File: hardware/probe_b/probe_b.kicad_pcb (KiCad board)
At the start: 2 copper layers, 81 x 20 mm, 30 parts, among them J1 TEST_1P, J3 TEST_1P, J4 TEST_1P, J5 TEST_1P, J7 Conn_01x04, Q1 SI3415, U1 ATTINY25-20PU

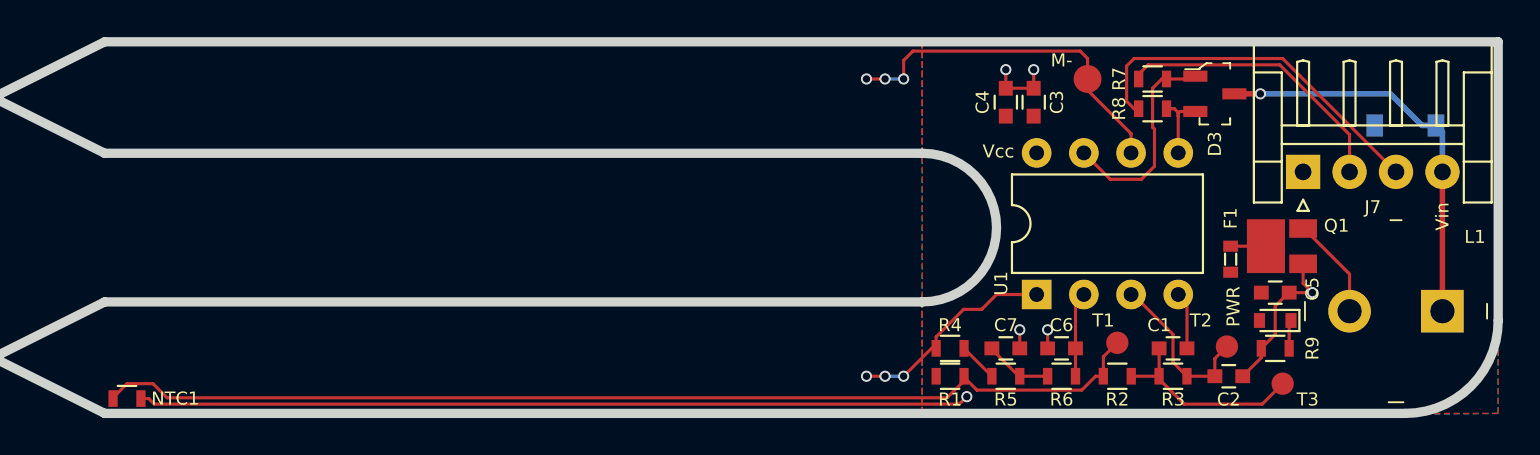
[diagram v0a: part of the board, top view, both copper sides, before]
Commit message: Fixes #21. Also removes RC filters that made the output impedence too high for the ADC. Changed connector to Micro USB due to cable availabiliy. Changed to a more reasonable inline ferrite and also removed ptc fuse due to too high Vdrop. Series resistors for I2C righ-sized.
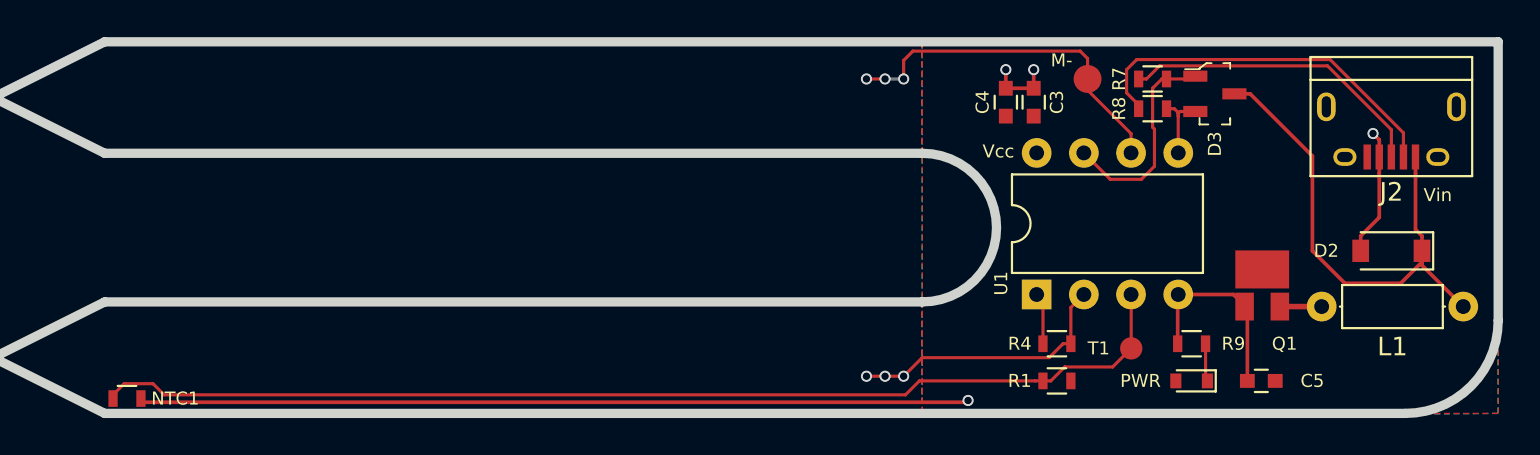
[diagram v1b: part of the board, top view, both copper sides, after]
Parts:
- removed C1, C2, C6, C7: 100nF, Capacitors_SMD:C_0603
- removed F1: Polyfuse_Small, digikey-footprints:0603
- removed J4, J5: TEST_1P, Measurement_Points:Measurement_Point_Round-SMD-Pad_Small
- removed J7: Conn_01x04, Connectors_JST:JST_EH_S04B-EH_04x2.50mm_Angled
- removed R2, R3, R5, R6: 100K, Resistors_SMD:R_0603
- added J2: USB_A, Connect:USB_Micro-B, F.Cu at (245.2, 104.8)
- D1: value LED -> PWR_LED
- D2: value D_Zener -> BZT52C5V6; moved to F.Cu
- D3: value BAT54C-7-F -> BAT54C
- L1: footprint digikey-footprints:Inductor_13R106C -> Inductors_THT:L_Axial_L5.3mm_D2.2mm_P7.62mm_Horizontal_Vishay_IM-1
- Q1: value SI3415 -> SI2323DS
- R1: value 10K -> 15K
- R7, R8: value R -> 33R
- R9: value 2K -> 1K
- moved D2 6.79 mm to (245.2, 111.2)
- moved R1 5.76 mm to (227.2, 118.2), turned to 180 degrees
- moved R4 5.76 mm to (227.2, 116.2)
- moved D1 5.55 mm to (234.5, 118.2)
- moved C5 4.81 mm to (238.2, 118.2), turned to 180 degrees
- moved R9 4.51 mm to (234.5, 116.2)
- moved L1 3.63 mm to (249.1, 114.2)
- moved Q1 2.55 mm to (238.3, 113.2), turned to 90 degrees
- moved J1 0.81 mm to (231.2, 116.5)
- moved G*** 0.34 mm to (231.5, 109.8)
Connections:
- J1 pad 1: Net-(J1-Pad1) -> TEMP_A
- NTC1 pad 1: Net-(J1-Pad1) -> TEMP_A
- Q1 pad 3: Net-(F1-Pad1) -> Vcc
- R1 pad 2: Net-(J1-Pad1) -> TEMP_A
- R4 pad 2: Net-(R4-Pad2) -> MOIST_A
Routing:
- net Net-(J1-Pad1): track 57.4 -> 0.00 mm
- net TEMP_A: track 9.08 -> 59.5 mm
- net MOIST_A: track 4.59 -> 15.6 mm, vias 0 -> 3
- net Net-(C1-Pad1): track 10.8 -> 0.00 mm
- net MOIST+: track 11.3 -> 3.04 mm, vias 3 -> 0
- net Vin: track 21.7 -> 27.7 mm, vias 1 -> 0
- net GND: track 61.9 -> 66.5 mm, vias 6 -> 4
- net Net-(C7-Pad1): track 3.65 -> 0.00 mm
- net Net-(L1-Pad2): track 5.51 -> 2.25 mm
- net Net-(R4-Pad2): track 2.12 -> 0.00 mm
- net Net-(F1-Pad1): track 1.90 -> 0.00 mm
- net Net-(J2-Pad3): track 15.4 -> 16.8 mm
- net Net-(J2-Pad2): track 19.9 -> 20.4 mm
- net Net-(D1-Pad1): track 1.54 -> 2.04 mm
- added copper zone on B.Cu, net MOIST_A
- added copper zone on F.Cu, net MOIST_A
- removed copper zone on B.Cu, net MOIST+
- removed copper zone on F.Cu, net MOIST+
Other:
- net class POWER: clearance 0.4 -> 0.2; trace_width 0.3 -> 0.2
- board text removed: "T2"
- board text removed: "T3"

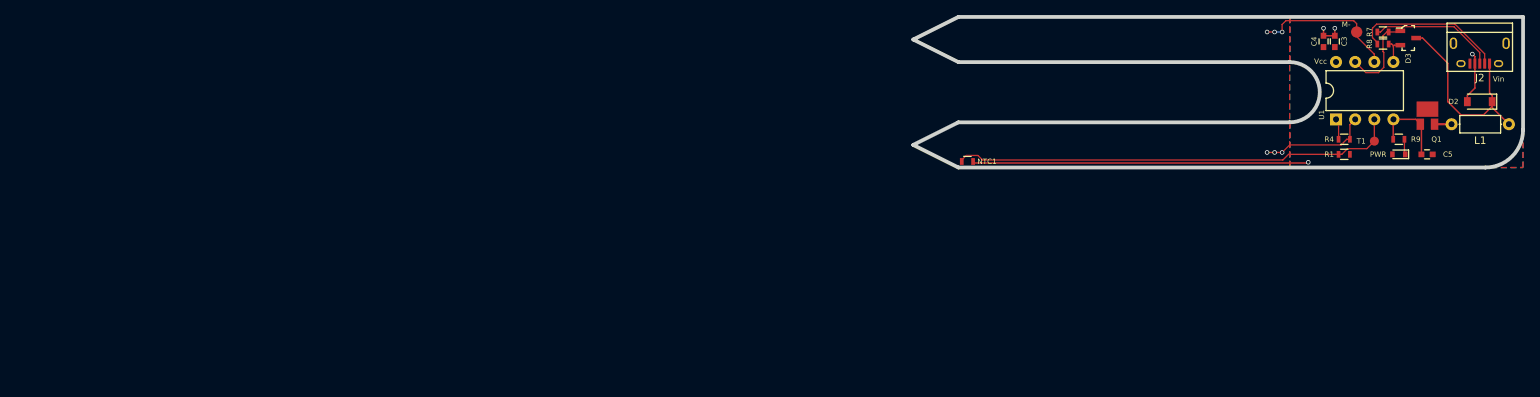
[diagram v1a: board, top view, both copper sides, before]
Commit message: Upgrading project to kicad 5.0 and fixing some issues with the last revision.
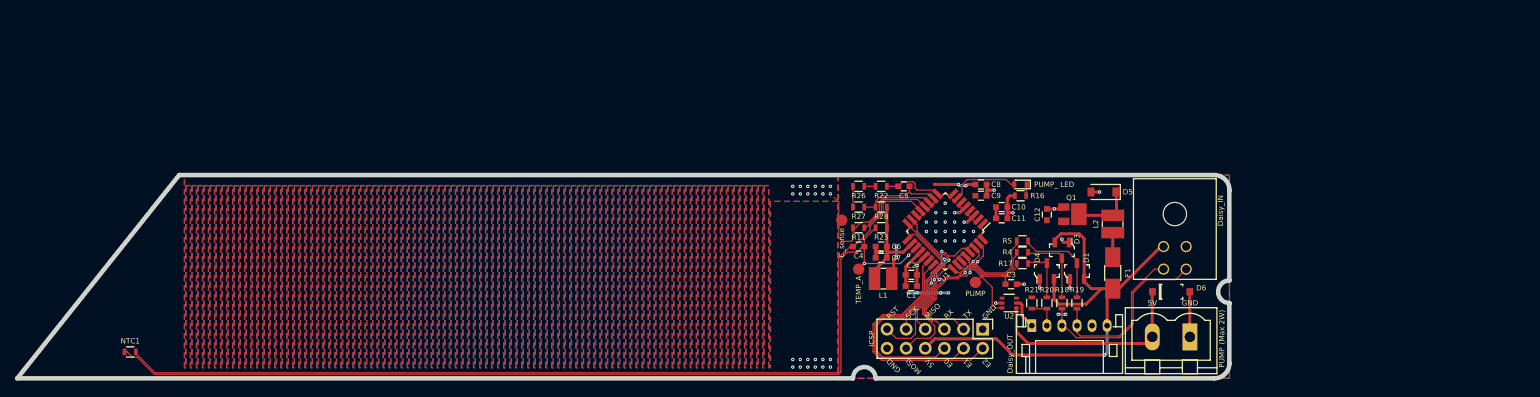
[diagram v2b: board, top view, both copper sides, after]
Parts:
- removed the G*** at (231.5, 109.8)
- removed R1: 15K, Resistors_SMD:R_0603
- removed R7, R8: 33R, Resistors_SMD:R_0603
- removed R9: 1K, Resistors_SMD:R_0603
- added C1: 10nF, Capacitors_SMD:C_0603, F.Cu at (169.8, 135.8)
- added C10: 10nF, Capacitors_SMD:C_0603, F.Cu at (181.8, 125.2)
- added C11: 100nF, Capacitors_SMD:C_0603, F.Cu at (181.8, 126.8)
- added C12: 1µF, Capacitors_SMD:C_0603, F.Cu at (187.8, 126.2)
- added C2: 100nF, Capacitors_SMD:C_0603, F.Cu at (169.8, 134.2)
- added C6: 10nF, Capacitors_SMD:C_0603, F.Cu at (165.8, 130.5)
- added C7: 100nF, Capacitors_SMD:C_0603, F.Cu at (165.8, 132.0)
- added C8: 100nF, Capacitors_SMD:C_0603, F.Cu at (179.0, 122.2)
- added C9: 10nF, Capacitors_SMD:C_0603, F.Cu at (179.0, 123.8)
- added D4: BAT54S-7-F, digikey-footprints:SOT-23-3, F.Cu at (187.8, 133.8)
- added D5: BZT52C5V6, Diodes_SMD:D_SOD-123, F.Cu at (195.2, 123.2)
- added D6: MBR0520LT1G, digikey-footprints:SOD-123, F.Cu at (204.2, 136.5)
- added F1: 0ZCJ0050FF2G, Fuse_Holders_and_Fuses:Fuse_SMD1206_HandSoldering, F.Cu at (196.5, 134.0)
- added G***: LOGO, emilibeda:waterino_8x16mm, B.Cu at (193.0, 130.2)
- added G***: LOGO, emilibeda:OSH_6mm, B.Cu at (156.5, 141.5)
- added J4: C_sense, Measurement_Points:Measurement_Point_Round-SMD-Pad_Small, F.Cu at (160.5, 127.0)
- added J5: Daisy_OUT, Connectors_JST:JST_PH_S6B-PH-K_06x2.00mm_Angled, F.Cu at (185.8, 141.0)
- added J6: Daisy_IN, Connectors_Molex:Molex_Microfit3_Header_02x02_Angled_43045-040x, F.Cu at (203.2, 130.5)
- added J7: TEMP_A, Measurement_Points:Measurement_Point_Round-SMD-Pad_Small, F.Cu at (162.8, 133.5)
- added L2: 10uH, digikey-footprints:1210, F.Cu at (196.5, 127.5)
- added R11: 1M, Resistors_SMD:R_0603, F.Cu at (162.8, 128.0)
- added R16: 1K, Resistors_SMD:R_0603, F.Cu at (184.2, 123.8)
- added R17: 150R, Resistors_SMD:R_0603, F.Cu at (184.5, 132.8)
- added R18: 150R, Resistors_SMD:R_0603, F.Cu at (189.8, 138.0)
- added R19: 150R, Resistors_SMD:R_0603, F.Cu at (191.8, 138.0)
- added R20: 150R, Resistors_SMD:R_0603, F.Cu at (187.8, 138.0)
- added R21: 10K, Resistors_SMD:R_0603, F.Cu at (185.8, 138.0)
- added R22: 100K, Resistors_SMD:R_0603, F.Cu at (165.8, 122.5)
- added R23: 15K, Resistors_SMD:R_0603, F.Cu at (165.8, 128.0)
- added R26: 100K, Resistors_SMD:R_0603, F.Cu at (162.8, 122.5)
- added R27: 100K, Resistors_SMD:R_0603, F.Cu at (162.8, 125.2)
- added R28: 100K, Resistors_SMD:R_0603, F.Cu at (165.8, 125.2)
- added R5: 150R, Resistors_SMD:R_0603, F.Cu at (184.5, 129.8)
- added U2: MIC94090, TO_SOT_Packages_SMD:SOT-363_SC-70-6, F.Cu at (182.8, 138.0)
- C5: value 1µF -> 100nF
- D1: value PWR_LED -> BAT54S-7-F; footprint Diodes_SMD:D_0603 -> digikey-footprints:SOT-23-3
- D2: value BZT52C5V6 -> PUMP_ LED; footprint Diodes_SMD:D_SOD-123 -> Diodes_SMD:D_0603
- D3: value BAT54C -> BAT54S-7-F
- J1: value TEST_1P -> ICSP; footprint Measurement_Points:Measurement_Point_Round-SMD-Pad_Small -> Pin_Headers:Pin_Header_Straight_2x06_Pitch2.54mm
- J2: value USB_A -> PUMP; footprint Connect:USB_Micro-B -> Measurement_Points:Measurement_Point_Round-SMD-Pad_Small
- J3: value TEST_1P -> PUMP; footprint Measurement_Points:Measurement_Point_Round-SMD-Pad_Small -> emilibeda:PhoenixContact_MSTBVA-G_02x5.00mm_Vertical
- L1: value L -> 10uH; footprint Inductors_THT:L_Axial_L5.3mm_D2.2mm_P7.62mm_Horizontal_Vishay_IM-1 -> digikey-footprints:1210
- R4: value 10K -> 150R
- U1: value ATTINY25-20PU -> ATMEGA328P-AU; footprint Housings_DIP:DIP-8_W7.62mm -> Housings_QFP:TQFP-32_7x7mm_Pitch0.8mm
- moved NTC1 114.0 mm to (66.0, 144.5)
- moved L1 85.6 mm to (166.0, 134.8)
- moved J2 73.6 mm to (178.2, 135.2), turned to 0 degrees
- moved C5 69.6 mm to (168.8, 122.5)
- moved C4 67.5 mm to (162.8, 130.5), turned to 0 degrees
- moved D2 62.0 mm to (184.2, 122.2)
- moved J1 57.7 mm to (179.2, 141.5), turned to 270 degrees
- moved U1 54.0 mm to (174.2, 128.5), turned to 225 degrees
- moved D3 54.0 mm to (189.8, 131.0), turned to 270 degrees
- moved C3 53.8 mm to (183.0, 135.5), turned to 0 degrees
- moved Q1 49.0 mm to (191.0, 126.2), turned to 0 degrees
- moved J3 46.2 mm to (206.8, 142.5), turned to 180 degrees
- moved D1 45.5 mm to (191.8, 133.8), turned to 90 degrees
- moved R4 45.3 mm to (184.5, 131.2), turned to 180 degrees
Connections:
- C3 pad 1: Vcc -> OVRFLW_SENSE
- C4 pad 1: Vcc -> ~TEMP_EXC
- C4 pad 2: GND -> TEMP+
- C5 pad 1: Vcc -> RC_REF
- C5 pad 2: GND -> ~RC_EXC
- D1 pad 1: Net-(D1-Pad1) -> GND
- D1 pad 2: Vcc -> Vin
- D2 pad 1: Vin -> Net-(D2-Pad1)
- D2 pad 2: GND -> PWRLED
- D3 pad 1: SCL -> GND
- D3 pad 2: SDA -> Vin
- D3 pad 3: Vin -> Net-(D3-Pad3)
- J1 pad 1: TEMP_A -> GND
- J2 pad 1: Vin -> PUMP
- J3 pad 1: MOIST- -> GND
- L1 pad 1: Vin -> Vcc
- L1 pad 2: Net-(L1-Pad2) -> AVcc
- NTC1 pad 1: TEMP_A -> TEMP+
- NTC1 pad 2: GND -> ~TEMP_EXC
- Q1 pad 2: Net-(L1-Pad2) -> Vcc
- Q1 pad 3: Vcc -> Net-(D5-Pad1)
- R4 pad 1: MOIST+ -> Net-(D3-Pad3)
- R4 pad 2: MOIST_A -> SDA
- U1 pad 1: MOIST+ -> Net-(U1-Pad1)
- U1 pad 2: MOIST_A -> Net-(U1-Pad2)
- U1 pad 3: TEMP_A -> GND
- U1 pad 4: GND -> Vcc
- U1 pad 5: SDA -> GND
- U1 pad 6: MOIST- -> Vcc
- U1 pad 7: SCL -> PWRLED
- U1 pad 8: Vcc -> Net-(U1-Pad8)
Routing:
- net TEMP+: track 0.00 -> 129.5 mm, vias 0 -> 2
- net ~TEMP_EXC: track 0.00 -> 125.5 mm
- net TEMP_A: track 59.5 -> 0.00 mm
- net Vin: track 27.7 -> 68.5 mm, vias 0 -> 1
- net DBG_A2: track 0.00 -> 32.2 mm
- net DBG_A1: track 0.00 -> 29.0 mm
- net Net-(D6-PadK): track 0.00 -> 28.3 mm
- net Net-(J5-Pad3): track 0.00 -> 25.6 mm
- net DBG_A0: track 0.00 -> 25.6 mm
- net GND: track 66.5 -> 41.0 mm, vias 4 -> 42
- net MOSI: track 0.00 -> 24.5 mm, vias 0 -> 2
- net /Csense: track 0.00 -> 23.2 mm, vias 0 -> 12
- net RST: track 0.00 -> 21.5 mm, vias 0 -> 2
- net Net-(J5-Pad4): track 0.00 -> 21.0 mm
- net Net-(J2-Pad2): track 20.4 -> 0.00 mm
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- added copper zone on B.Cu, net /Csense
- added copper zone on F.Cu, net /Csense
- added copper zone on F.Cu, net GND
- removed copper zone on B.Cu, net MOIST-
- removed copper zone on F.Cu, net MOIST-
- removed copper zone on B.Cu, net MOIST_A
- removed copper zone on F.Cu, net MOIST_A
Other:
- board size 81 x 20 mm -> 161 x 27 mm
- net class Default: clearance 0.17 -> 0.11; trace_width 0.17 -> 0.11; via_dia 0.6 -> 0.45; via_drill 0.4 -> 0.2
- net class POWER removed
- net class Power added: clearance 0.15, trace_width 0.4, via_dia 0.45, via_drill 0.2
- rule pad_to_mask_clearance: 0.01 -> 0
- rule trace_clearance: 0.17 -> 0.11
- rule trace_min: 0.16 -> 0.11
- rule via_min_drill: 0.3 -> 0.2
- rule via_min_size: 0.4 -> 0.45
- board text added: "(Max 2W)"
- board text added: "1809"
- board text added: "5V"
- board text added: "Designed for 2-layer, 100 µm process with 10% added tolerance and 300 µm edge clearance."
- board text added: "E0"
- board text added: "E1"
- board text added: "E2"
- board text added: "GND"
- board text added: "MISO"
- board text added: "MOSI"
- board text added: "Probe C Rev 1"
- board text added: "RST"
- board text added: "RX"
- board text added: "SCK"
- board text added: "TX"
- board text added: "Waterino"
- board text added: "github.com/EmilyBjoerk/Waterino"
- board text removed: "All components and traces besides the connector and two electrodes shall be covered in a moisture and corrosion proof conformal coating. The device it self shall be put in a housing which protects the connector from water splashes (IP level 4). Alternatively you can dip-coat the the device with a device wires attached (in which case you can skip the connector and solder the wires directly to save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"
- board text removed: "M-"
- board text removed: "PWR"
- board text removed: "T1"
- board text removed: "The device is designed with a 0.16mm (6 mil) minimum feature size. Where possible extra clearance has been given. The electrodes must have ENIG coating, otherwise they will corrode rapidly. Program the ATiny on a bread board prior to installation. A socket can be used but is not recommended as moisture can creep between the IC and socket and cause long term damage."
- board text removed: "Vcc"
- board text removed: "Vin"
- board text removed: "Waterino Probe B Rev 1"
